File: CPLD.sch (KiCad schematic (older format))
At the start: 53 parts, among them J4 JTAG, J5 PMOD, Q1 IRLML6402, Q2 IRLML6402, U6 EPM7064STC100, X1 CFPS-72 50mhz

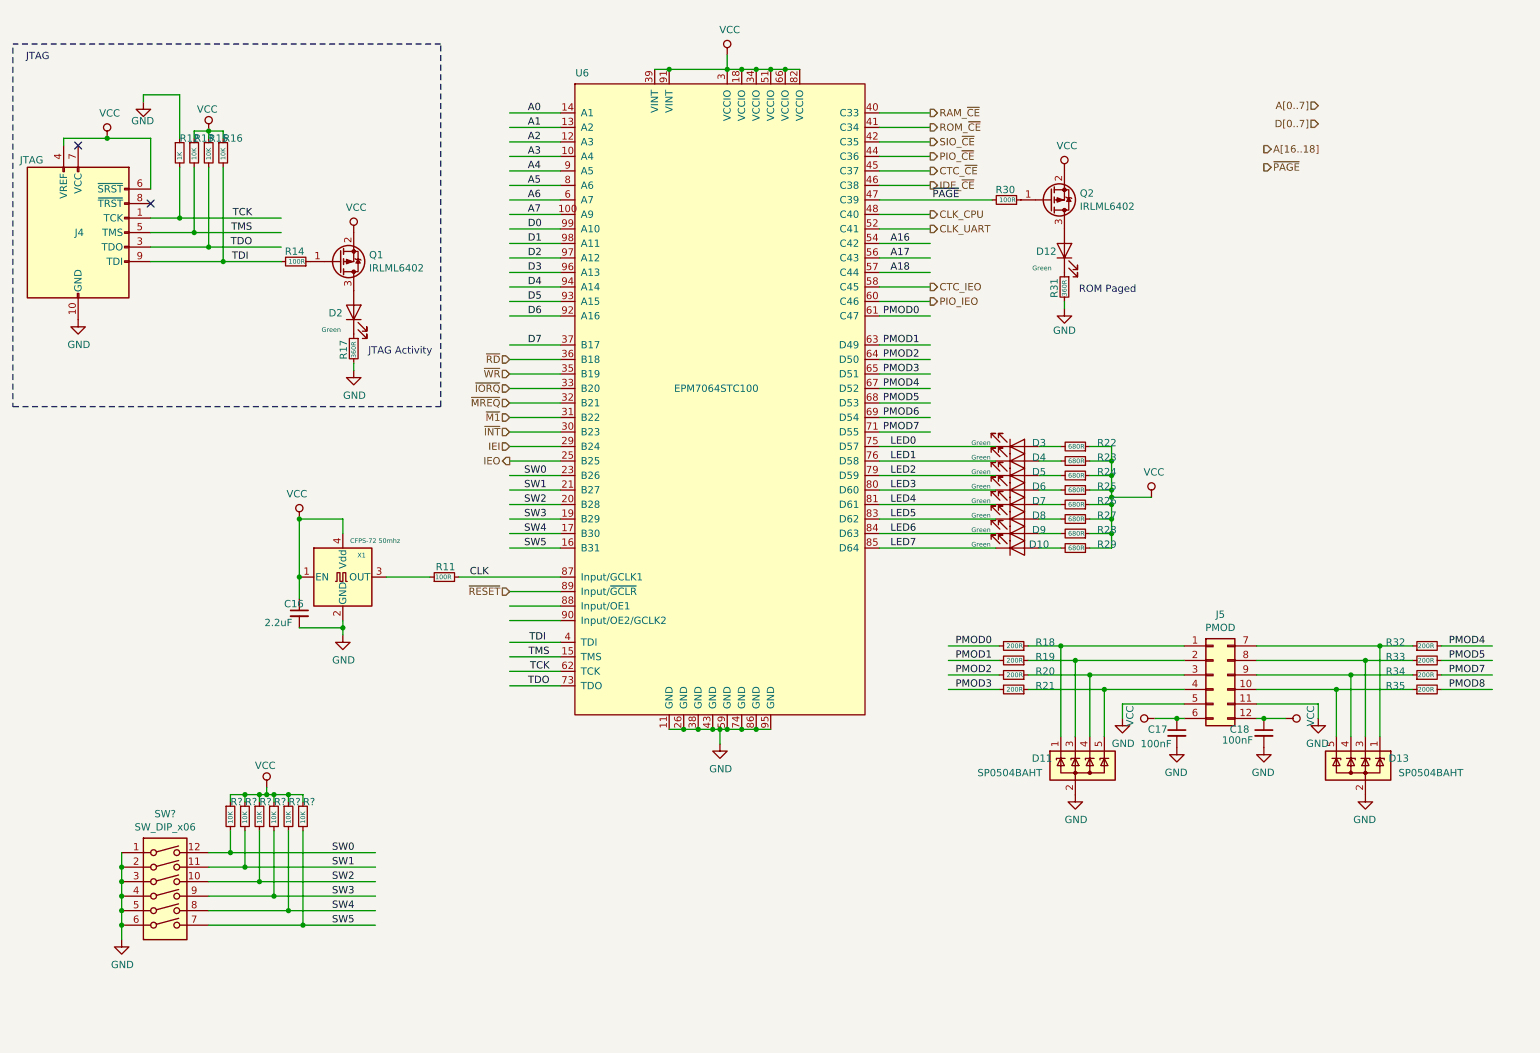
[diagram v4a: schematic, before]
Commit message: connected sheet pins to bus
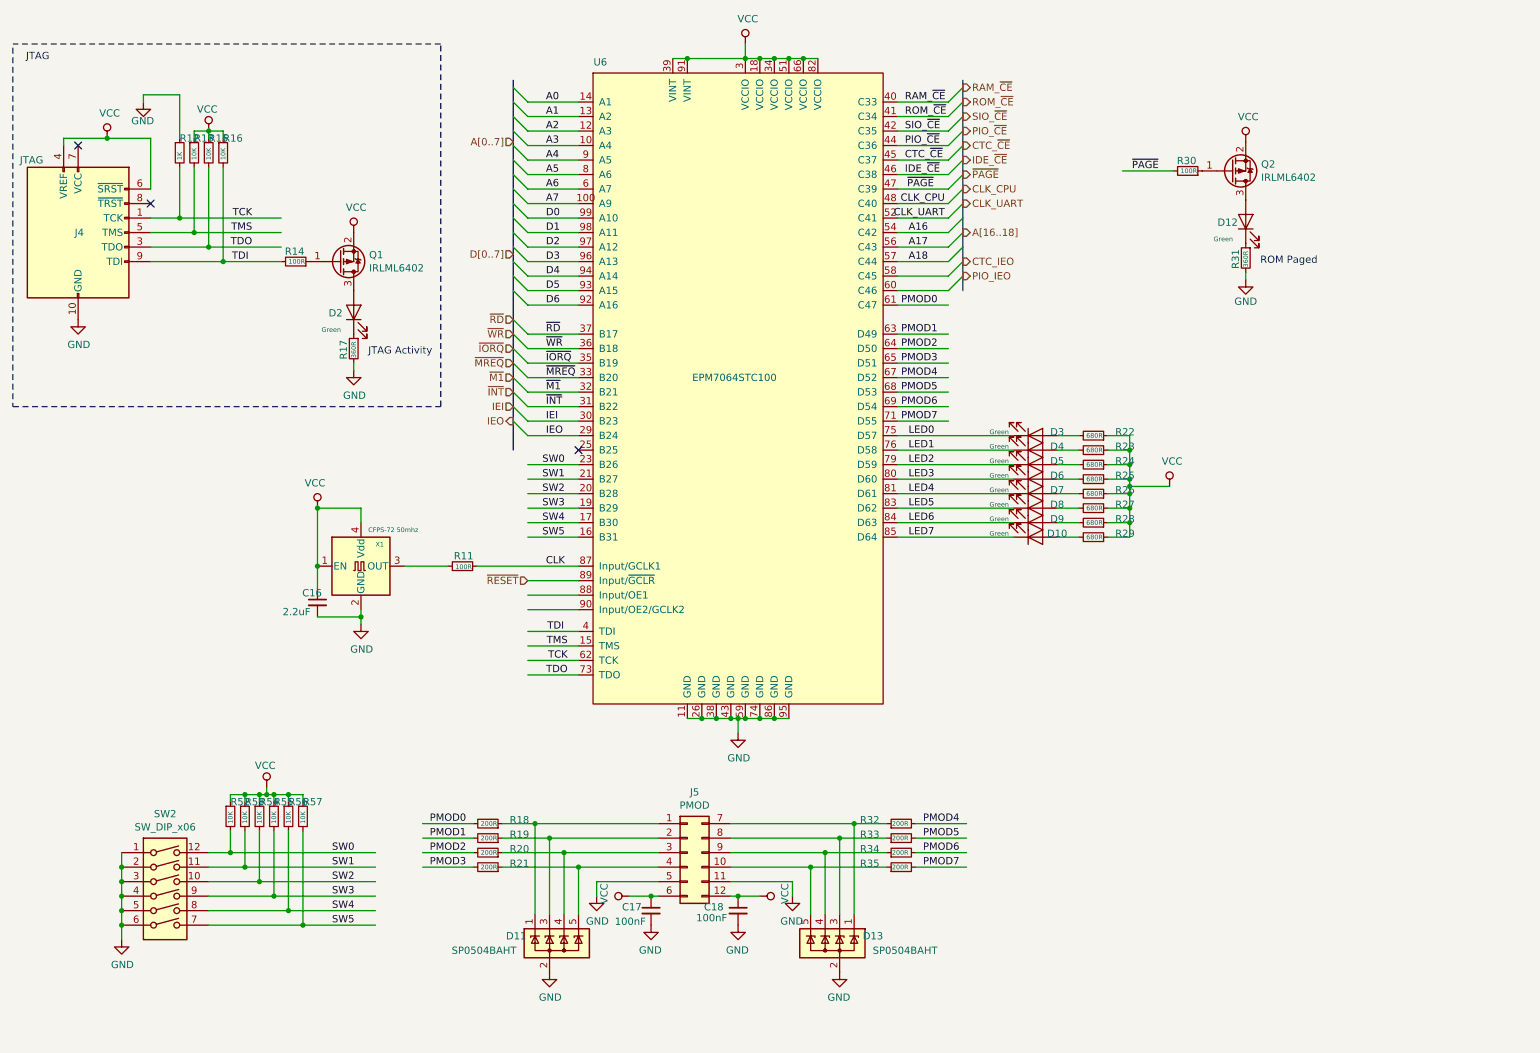
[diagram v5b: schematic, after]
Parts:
- SW2: renamed from SW?; footprint (none) -> Button_Switch_SMD:SW_DIP_SPSTx06_Slide_6.7x16.8mm_W6.73mm_P2.54mm_LowProfile_JPin
- gave numbers to parts that had none: 6
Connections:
- net labels removed: D7, PMOD8
- no-connect marks 2 -> 3
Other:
- moved on the sheet: C16, C17, C18, D10, D11, D12, D13, D3, D4, D5, D6, D7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

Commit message: Moved CPU, RAM, ROM to sub-sheet
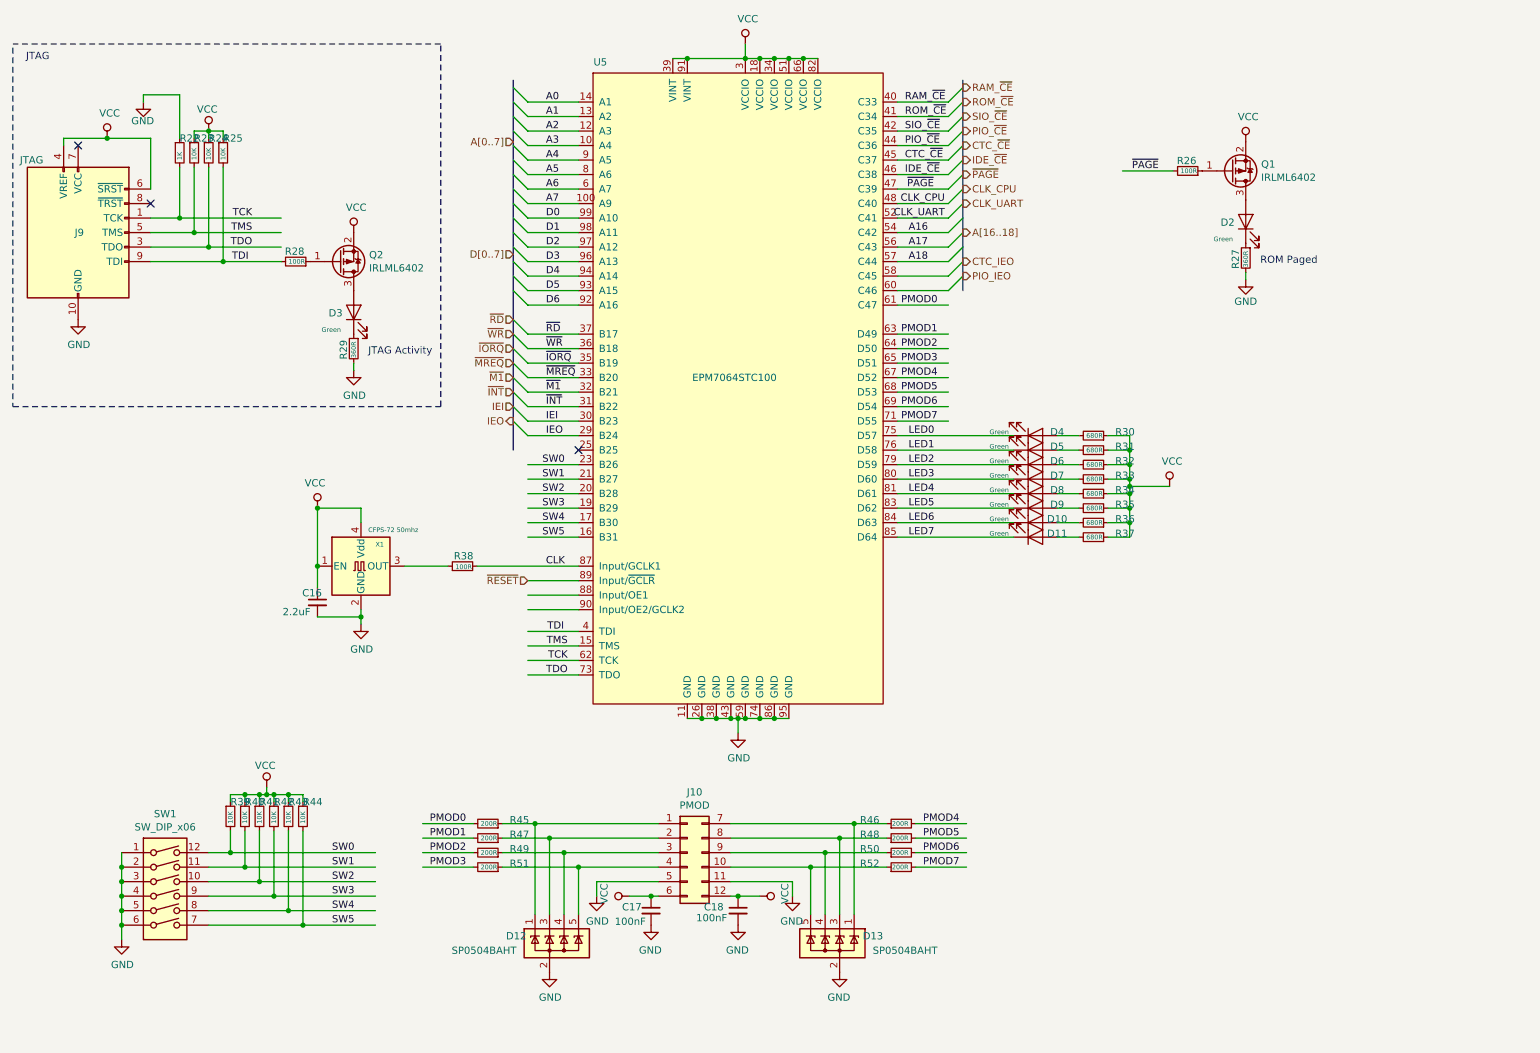
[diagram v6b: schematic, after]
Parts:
- renumbered D9 to D10, D10 to D11, D11 to D12, D12 to D2, D2 to D3, D3 to D4, D4 to D5, D5 to D6, D6 to D7, D7 to D8, D8 to D9, J5 to J10, J4 to J9, Q2 to Q1, Q1 to Q2, R12 to R22, R13 to R23, R15 to R24, R16 to R25, R30 to R26, R31 to R27, R14 to R28, R17 to R29, R22 to R30, R23 to R31, R24 to R32, R25 to R33, R26 to R34, R27 to R35, R28 to R36, R29 to R37, R11 to R38, R52 to R39, R53 to R40, R54 to R41, R55 to R42, R56 to R43, R57 to R44, R18 to R45, R32 to R46, R19 to R47, R33 to R48, R20 to R49, R34 to R50, R21 to R51, R35 to R52, SW2 to SW1, U6 to U5

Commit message: fixed bus connections
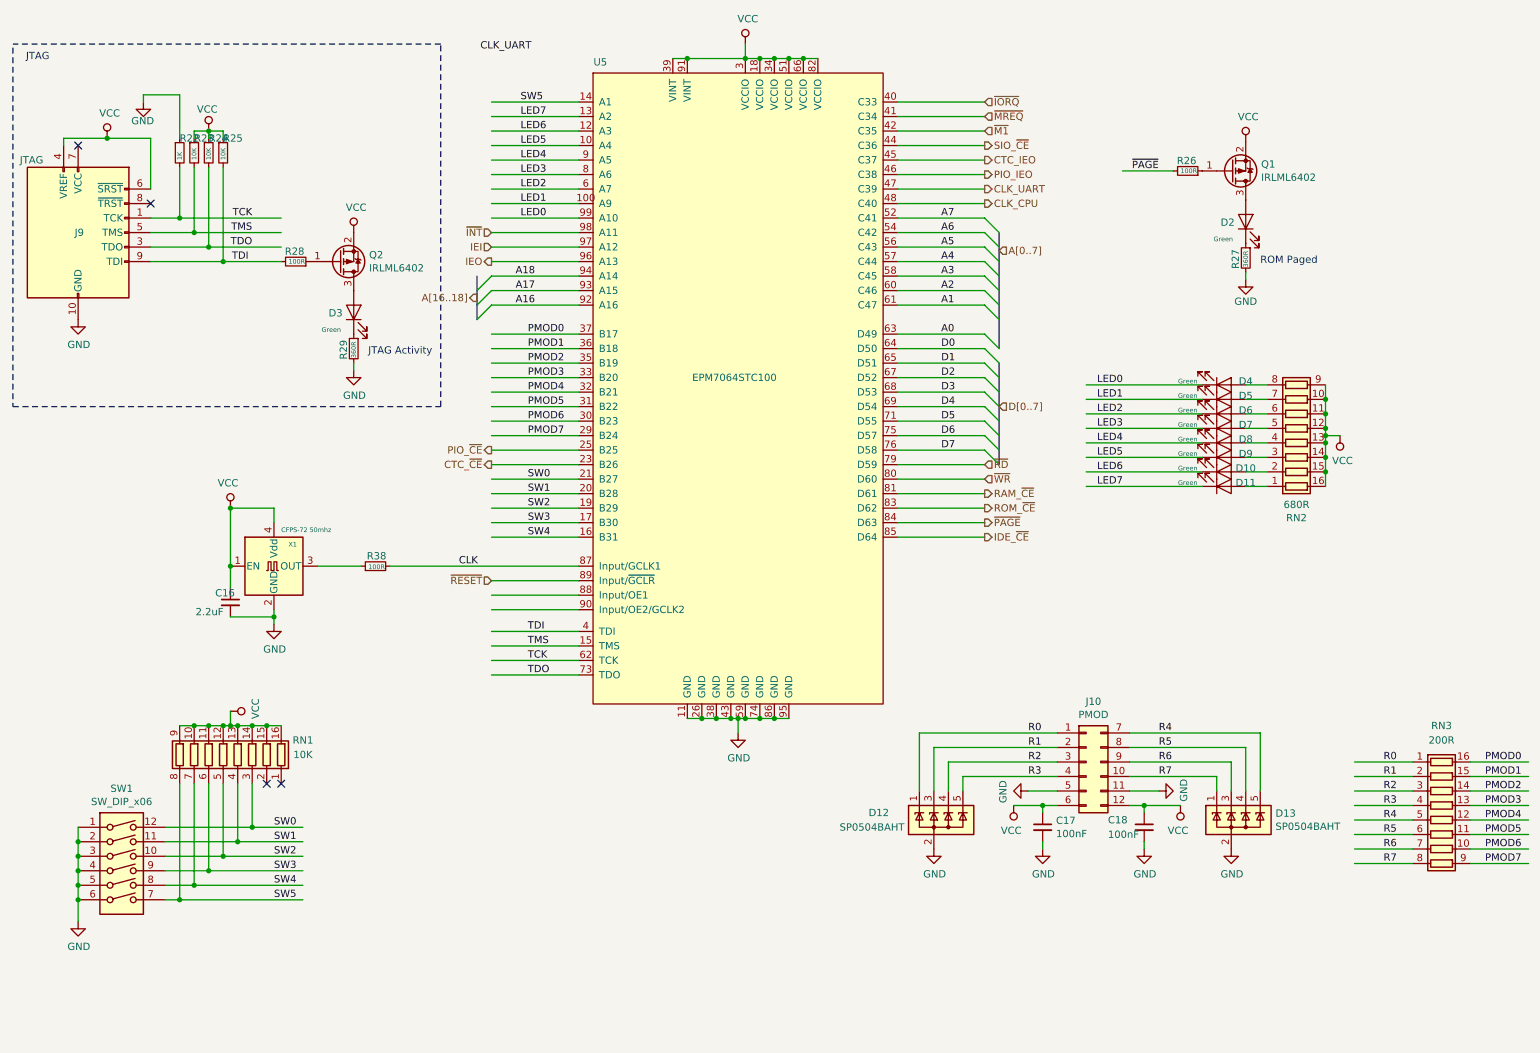
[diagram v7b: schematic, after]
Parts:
- removed R30, R31, R37: 680R, Resistor_SMD:R_0603_1608Metric_Pad1.05x0.95mm_HandSolder, symbol Device:R_Small
- removed R32, R33, R34, R35, R36: 680R, Resistor_SMD:R_0603_1608Metric_Pad1.05x0.95mm_HandSolder, symbol THS-80-rescue:R_Small-Device-sbc_z80-rescue
- removed R39, R40, R41, R42, R43, R44: 10K, Resistor_SMD:R_0603_1608Metric_Pad1.05x0.95mm_HandSolder, symbol Device:R_Small
- removed R45, R46, R47, R48, R49, R50, R51, R52: 200R, Resistor_SMD:R_0603_1608Metric_Pad1.05x0.95mm_HandSolder, symbol Device:R_Small
- added RN1: 10K, Resistor_SMD:R_Cat16-8, symbol Device:R_Pack08
- added RN2: 680R, Resistor_SMD:R_Cat16-8, symbol Device:R_Pack08
- added RN3: 200R, Resistor_SMD:R_Cat16-8, symbol Device:R_Pack08
- D12, D13: Description ESD Suppressors / TVS Diodes SP0504BAHTG -> (none); MFR Littelfuse -> (none); MPN SP0504BAHTG -> (none); SPN 576-SP0504BAHTG -> (none); SPR Mouser -> (none); SPURL https://www.mouser.com/ProductDetail/576-SP0504BAHTG -> (none)
- SW1: footprint Button_Switch_SMD:SW_DIP_SPSTx06_Slide_6.7x16.8mm_W6.73mm_P2.54mm_LowProfile_JPin -> Button_Switch_SMD:SW_DIP_SPSTx06_Slide_Omron_A6S-610x_W8.9mm_P2.54mm
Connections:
- net labels added: D7, R0, R1, R2, R3, R4, R5, R6, R7
- wire segments 221 -> 220
- no-connect marks 3 -> 4
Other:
- moved on the sheet: C16, D10, D11, D4, D5, D6, D7, D8, D9, R38, X1

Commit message: passed DRC
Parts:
- added C10, C11, C12, C13, C6, C7, C8, C9: 100nF, Capacitor_SMD:C_0603_1608Metric_Pad1.05x0.95mm_HandSolder, symbol Device:C_Small
- added R17, R18: 10K, Resistor_SMD:R_0603_1608Metric_Pad1.05x0.95mm_HandSolder, symbol Device:R_Small
- renumbered C17 to C14, C18 to C15, C16 to C5, D13 to D12, D2 to D13, D3 to D2, D12 to D3, J9 to J5, J10 to J6, Q2 to Q1, Q1 to Q2, R22 to R10, R23 to R11, R24 to R12, R25 to R13, R28 to R14, R29 to R15, R38 to R16, R26 to R19, R27 to R20, SW1 to SW2, U5 to U3
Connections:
- net labels added: ~WAIT
- net labels removed: CTC_IEO, IEI, IEO, PIO_IEO, ~INT
- wire segments 220 -> 238
- no-connect marks 4 -> 8
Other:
- moved on the sheet: C14, C15, D10, D11, D12, D3, D4, D5, D6, D7, D8, D9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
